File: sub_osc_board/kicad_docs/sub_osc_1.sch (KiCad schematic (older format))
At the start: 25 parts, among them Q1 MMBF5457, Q2 MMBF5457, U1 TL072, U2 TL072, U3 TL072, U7 40106, U8 4013

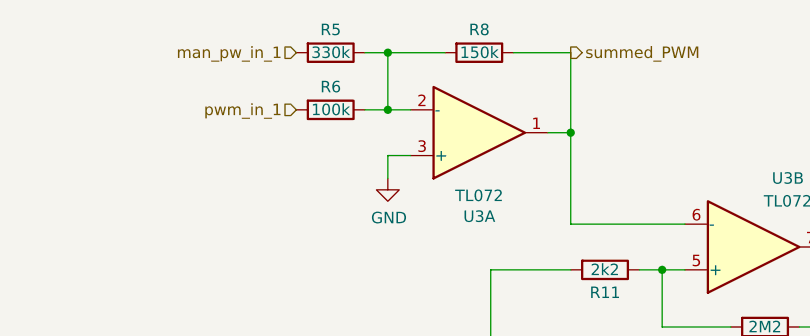
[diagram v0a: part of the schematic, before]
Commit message: change sub-osc PWM range and mixer gain
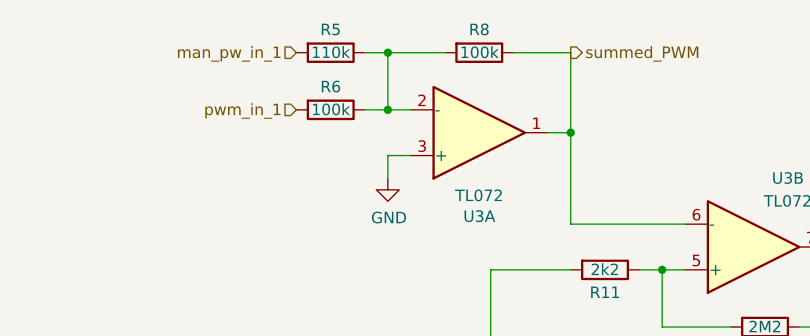
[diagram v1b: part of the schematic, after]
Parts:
- R5: value 330k -> 110k
- R8: value 150k -> 100k
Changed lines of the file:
@@
 AR Path="/5EE658F9/5EF8121A" Ref="R?"  Part="1"
 F 0 "R8" V 6600 1350 50  0000 C CNN
-F 1 "150k" V 6700 1350 50  0000 C CNN
+F 1 "100k" V 6700 1350 50  0000 C CNN
 F 2 "Resistor_SMD:R_0805_2012Metric_Pad1.15x1.40mm_HandSolder" V 6630 1350 50  0001 C CNN
 F 3 "~" H 6700 1350 50  0001 C CNN
@@
 AR Path="/5EE658F9/5EF8122D" Ref="R?"  Part="1"
 F 0 "R5" V 5950 1350 50  0000 C CNN
-F 1 "330k" V 6050 1350 50  0000 C CNN
+F 1 "110k" V 6050 1350 50  0000 C CNN
 F 2 "Resistor_SMD:R_0805_2012Metric_Pad1.15x1.40mm_HandSolder" V 5980 1350 50  0001 C CNN
 F 3 "~" H 6050 1350 50  0001 C CNN
